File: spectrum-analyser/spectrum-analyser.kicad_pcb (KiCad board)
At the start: 2 copper layers, 50 x 95 mm, 40 parts, among them J1 Conn_Coaxial, J2 Conn_01x02, Q1 PMOS, Q2 PMOS, Q3 Q_PMOS_GSD, Q4 Q_NMOS_GSD, Q5 Q_NMOS_GSD, SW1 SW_SPDT, SW2 SW_UP, SW3 SW_RIGHT, SW4 SW_LEFT, SW5 SW_DOWN, U1 1.3" OLED, U2 ESP32-C3_Zero, U3 LM1117MP-3.3, U4 RX5808(V3.3), U5 AP9101CK6, U6 MCP73831-2-OT

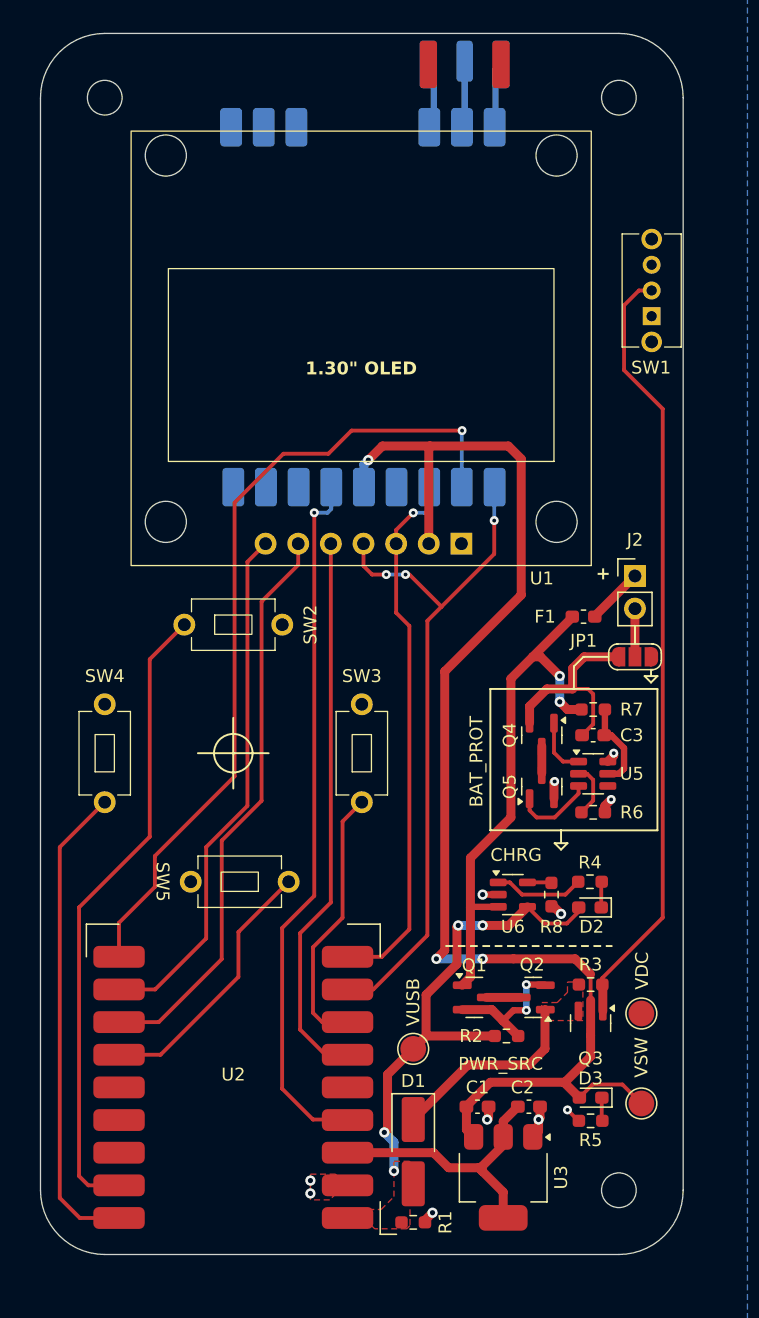
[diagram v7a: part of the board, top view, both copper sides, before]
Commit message: Add informational silkscreen and change 3v3 LDO package
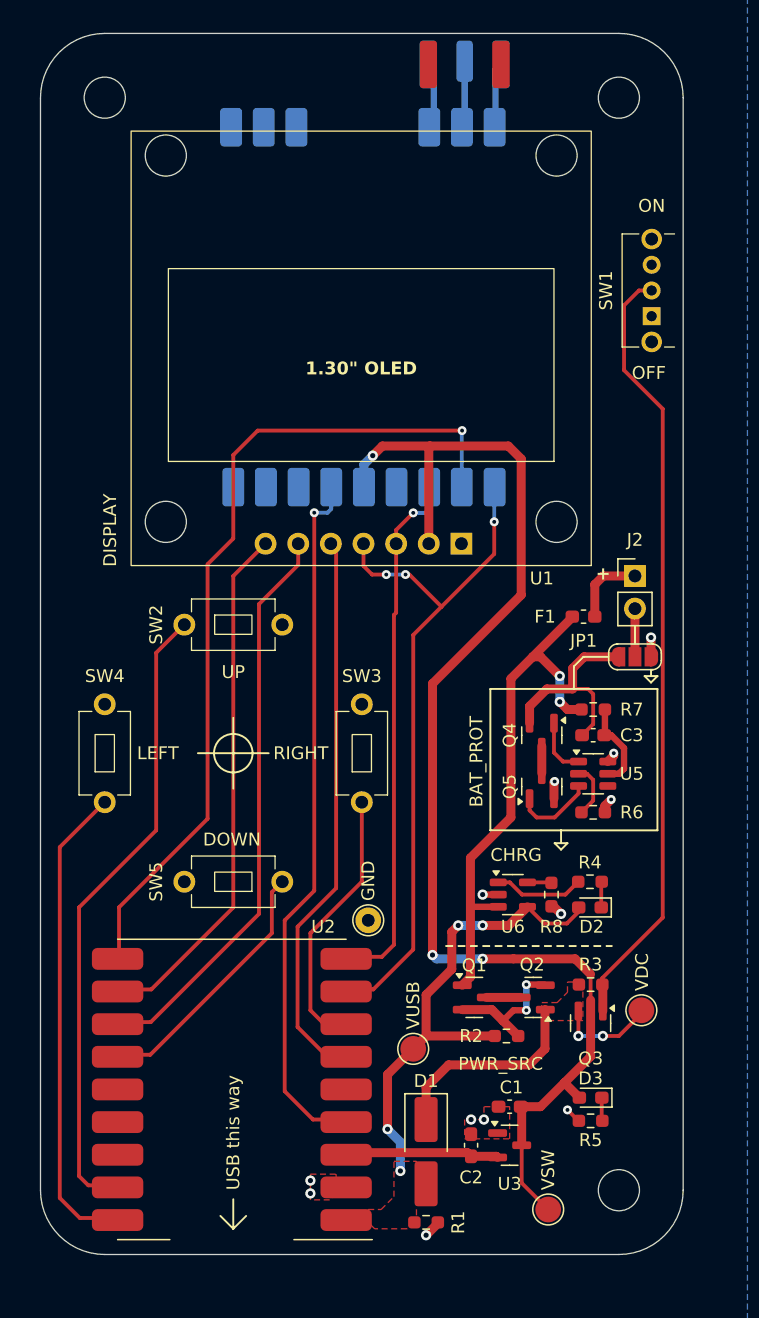
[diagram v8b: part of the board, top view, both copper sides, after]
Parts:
- added TP4: TestPoint, TestPoint:TestPoint_THTPad_D2.0mm_Drill1.0mm, F.Cu at (120.5, 129.0)
- H1, H2, H3: footprint MountingHole:MountingHole_2.7mm_M2.5 -> MountingHole:MountingHole_3.2mm_M3_ISO7380
- U3: value LM1117MP-3.3 -> AP2127N-3.3; footprint Package_TO_SOT_SMD:SOT-223-3_TabPin2 -> Package_TO_SOT_SMD:SOT-23
- moved TP3 11.0 mm to (134.5, 151.5)
- moved C2 5.41 mm to (128.5, 146.5), turned to 90 degrees
- moved U3 2.55 mm to (131.5, 146.5), turned to 0 degrees
- moved C1 2.50 mm to (131.5, 143.5), turned to 180 degrees
- moved D1 1.00 mm to (125.0, 147.0)
- moved R1 1.00 mm to (125.0, 152.5)
- moved SW5 0.50 mm to (110.0, 126.0)
- moved TP2 0.25 mm to (141.8, 136.0)
- moved U2 0.19 mm to (109.9, 142.2)
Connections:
- SW1 pad 1: GND -> unconnected-(SW1-A-Pad1)
- SW1 pad 3: unconnected-(SW1-C-Pad3) -> GND
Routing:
- net +3V3: track 21.5 -> 11.8 mm
- net VDC: track 15.6 -> 23.6 mm, vias 0 -> 2
- net +VSW: track 104.8 -> 101.0 mm
- net RX_CS: track 63.5 -> 65.7 mm
- net GND: track 22.1 -> 20.4 mm, vias 11 -> 12
- net /Battery management/BAT_CONN_POS: track 4.46 -> 5.90 mm
- net SPI_CLK: track 42.1 -> 41.3 mm
- net BTN_DOWN: track 20.8 -> 20.1 mm
- net DISPLAY_RST: track 43.3 -> 43.8 mm
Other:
- board text added: "3V3"
- board text added: "BTN_DOWN"
- board text added: "BTN_LEFT"
- board text added: "BTN_RIGHT"
- board text added: "BTN_UP"
- board text added: "CS DC RST MOSI CLK VSW GND"
- board text added: "DISPLAY"
- board text added: "DISP_CS"
- board text added: "DISP_DC"
- board text added: "DISP_RST"
- board text added: "DOWN"
- board text added: "GND"
- board text added: "GND x x RSSI V+ GND CLK CS MOSI"
- board text added: "LEFT"
- board text added: "OFF"
- board text added: "ON"
- board text added: "RECV"
- board text added: "RIGHT"
- board text added: "RSSI"
- board text added: "RX_CS"
- board text added: "SMA"
- board text added: "SPI_CLK"
- board text added: "SPI_MOSI"
- board text added: "UP"
- board text added: "USB this way"
